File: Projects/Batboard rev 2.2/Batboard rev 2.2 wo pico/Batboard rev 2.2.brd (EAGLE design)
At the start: 101.6 x 68.6 mm, 63 parts, among them J1 1X2-3.5MM, J2 1X2-3.5MM, J3 1X2-3.5MM, J4 1X2-3.5MM, J5 1X2-3.5MM, J6 1X2-3.5MM, U2 TL3472CD, X1 22-23-2081, X17 22-23-2081

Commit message: Not sure
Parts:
- added LED1, LED2, LED3, LED4: (no value), eagle-ltspice:LED_1206
- added R1, R11, R13, R4: 1K, adafruit:M1206
- added U$9: DMN2004DMK_DUAL_N-CHANNEL_MOSFET_ARRAY, ultravolt_daughterboard:SOT23-6
- moved SV1 13.7 mm to (4.60, 7.62)
- moved U$8 2.90 mm to (4.92, 33.0)
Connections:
- new net 10V: U$1.17, U$1.18, U$8.2
- new net N$31: LED1.A, U$8.6
- new net N$84: LED2.A, U$8.3
- new net N$85: LED3.A, U$9.6
- new net N$86: LED4.A, U$9.3
- new net N$87: LED2.C, R4.2
- new net N$88: LED3.C, R11.2
- new net N$89: LED4.C, R13.2
- net +12V: now also U$9.5
- net +5V: now also R1.1, R11.1, R4.1, U$8.5, U$9.2
- net -12V: now also U$9.1
- net GND: now also R13.1, U$8.1, U$8.4, U$9.4
- net N$1: now also LED1.C, R1.2; no longer U$1.17, U$1.18
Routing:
- net -12V: track 49.1 -> 110.8 mm
- net +12V: track 226.4 -> 233.2 mm
- net N$1: track 2.54 -> 0.00 mm
- net 10V: track 0.00 -> 2.54 mm

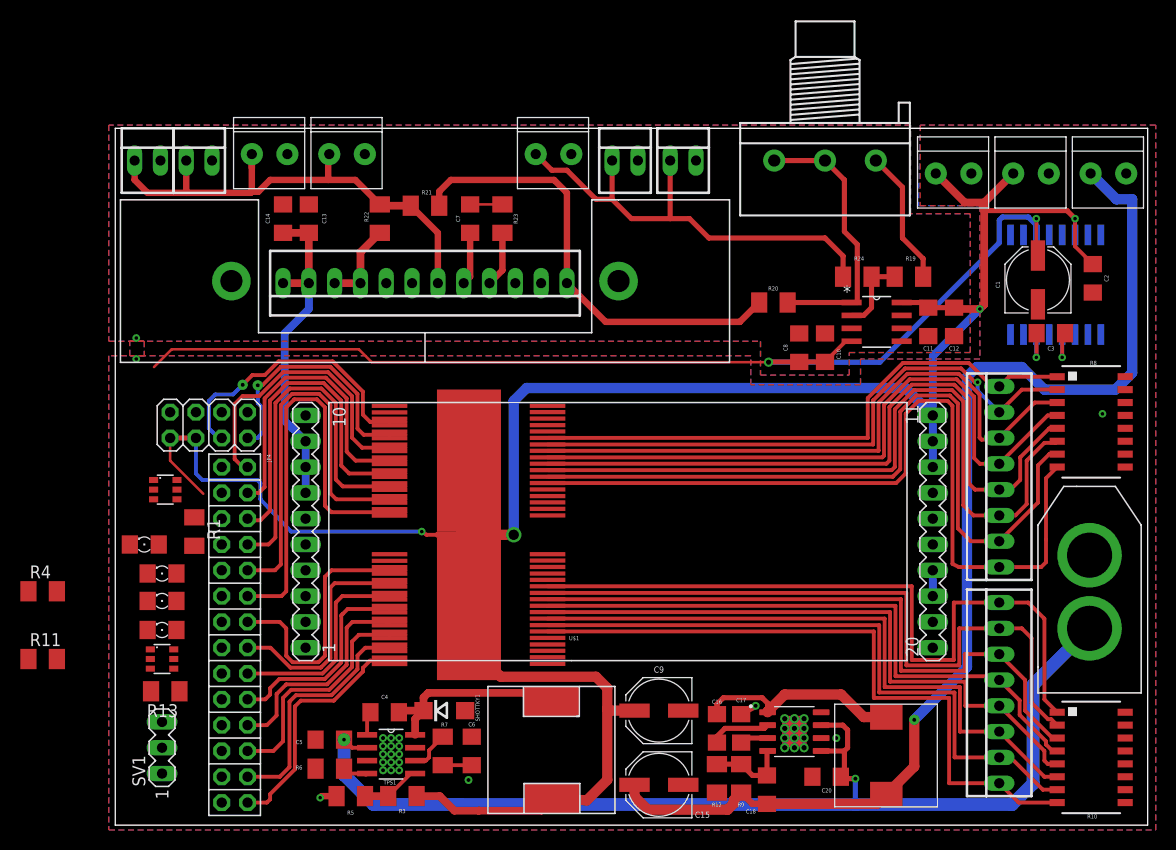
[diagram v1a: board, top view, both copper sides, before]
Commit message: Fixed back to "Updated LEDs"
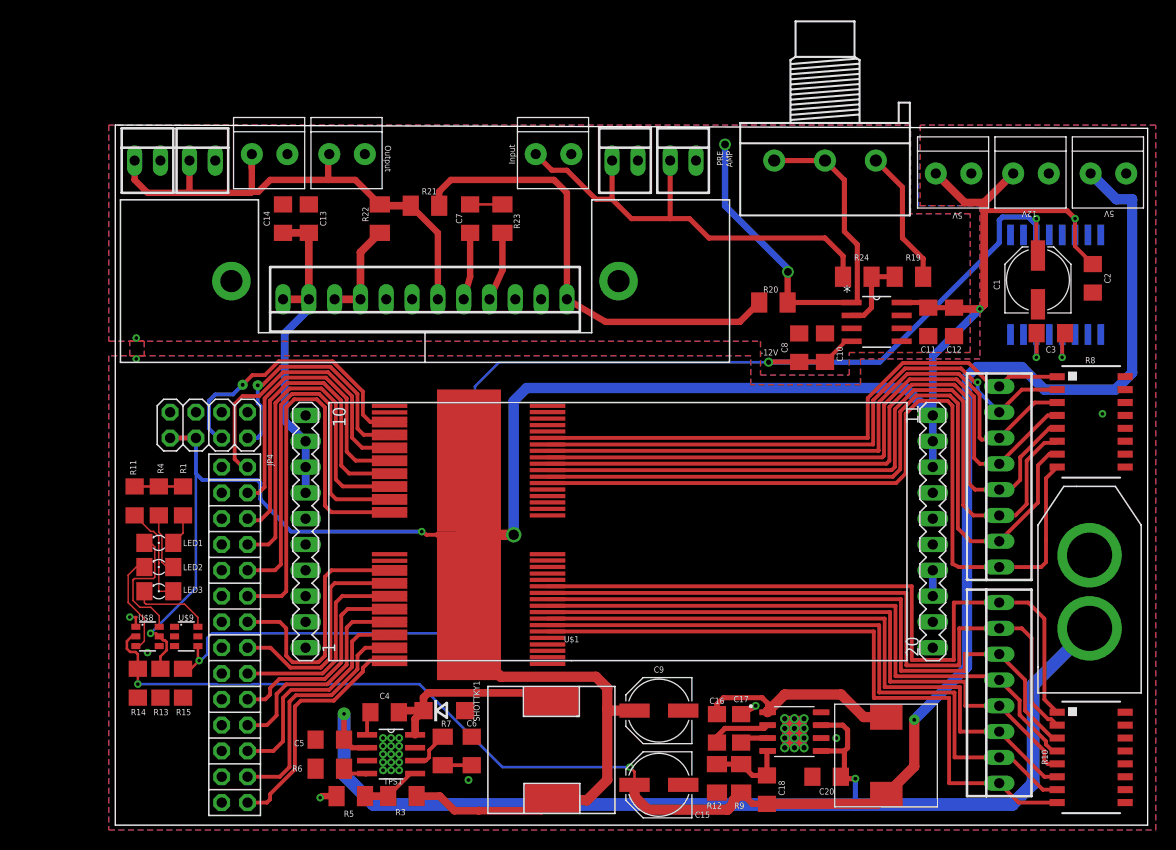
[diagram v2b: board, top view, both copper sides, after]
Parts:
- removed LED4: (no value), eagle-ltspice:LED_1206
- removed SV1: (no value), con-lstb:MA03-1
- added R14, R15: 1K, resistor:R1206
- R1, R11, R4: value 1K -> 500; device adafruit:M1206 -> resistor:R1206
- R13: device adafruit:M1206 -> resistor:R1206
- R2: value (none) -> 50K
- moved R11 18.0 mm to (1.91, 31.9), turned to 90 degrees
- moved U$8 14.6 mm to (3.17, 18.6)
- moved R4 14.5 mm to (4.29, 31.9), turned to 90 degrees
- moved U$9 3.26 mm to (6.99, 18.6)
- moved R1 3.21 mm to (6.67, 31.9), turned to 90 degrees
- moved PIN1 1.59 mm to (30.5, 51.8)
- moved LED1 1.44 mm to (4.29, 27.8)
- moved LED3 1.00 mm to (4.29, 23.0)
- moved R13 0.93 mm to (4.45, 14.0), turned to 90 degrees
- moved LED2 0.71 mm to (4.29, 25.4)
- moved S1 0.32 mm to (8.57, 65.4)
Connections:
- removed net 10V: U$1.17, U$1.18, U$8.2
- removed net N$89: LED4.C, R13.2
- new net 5V: R1.2, R11.2, R4.2
- net +12V: now also R13.2, U$8.5; no longer U$9.5
- net +5V: now also R14.2, U$8.2; no longer R1.1, R11.1, R4.1, U$8.5, U$9.2
- net -12V: now also R15.1, U$9.4; no longer U$9.1
- net GND: now also R14.1, R15.2, U$9.5; no longer U$9.4
- net N$1: now also U$1.17, U$1.18; no longer LED1.C, R1.2
- net N$31: now also R1.1; no longer U$8.6
- net N$84: now also R4.1; no longer U$8.3
- net N$85: now also R11.1; no longer U$9.6
- net N$86: now also LED3.C, U$9.6; no longer LED4.A, U$9.3
- net N$87: now also LED1.C, U$8.6; no longer LED2.C, R4.2
- net N$88: now also LED2.C, U$8.3; no longer LED3.C, R11.2
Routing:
- net +5V: track 113.8 -> 173.6 mm, vias 1 -> 3
- net -12V: track 110.8 -> 133.9 mm, vias 2 -> 3
- net +12V: track 233.2 -> 252.3 mm, vias 4 -> 5
- net N$15: track 27.1 -> 45.4 mm, vias 0 -> 2
- net N$87: track 0.00 -> 12.7 mm
- net N$88: track 0.00 -> 10.1 mm
- net N$85: track 0.22 -> 10.0 mm
- net N$86: track 0.00 -> 7.91 mm
- net N$84: track 0.00 -> 6.67 mm
- net BATT: track 108.2 -> 113.3 mm
- net 5V: track 0.00 -> 4.76 mm
- net N$31: track 0.00 -> 3.10 mm
- net N$1: track 0.00 -> 2.54 mm
- net 10V: track 2.54 -> 0.00 mm
- net GND: track 3.34 -> 4.95 mm, vias 7 -> 9
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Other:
- board size 101.6 x 68.6 mm -> 101.6 x 68.9 mm
- board text added: "-12V"
- board text added: "12V"
- board text added: "5V"
- board text added: "Input"
- board text added: "Output"
- board text added: "PRE AMP"
